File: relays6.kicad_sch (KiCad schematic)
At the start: 1 part

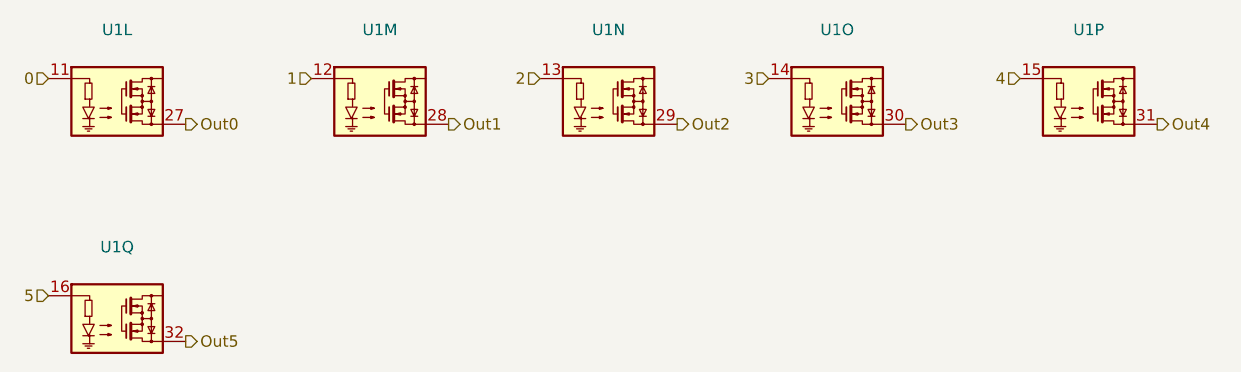
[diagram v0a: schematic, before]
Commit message: added module for PSU
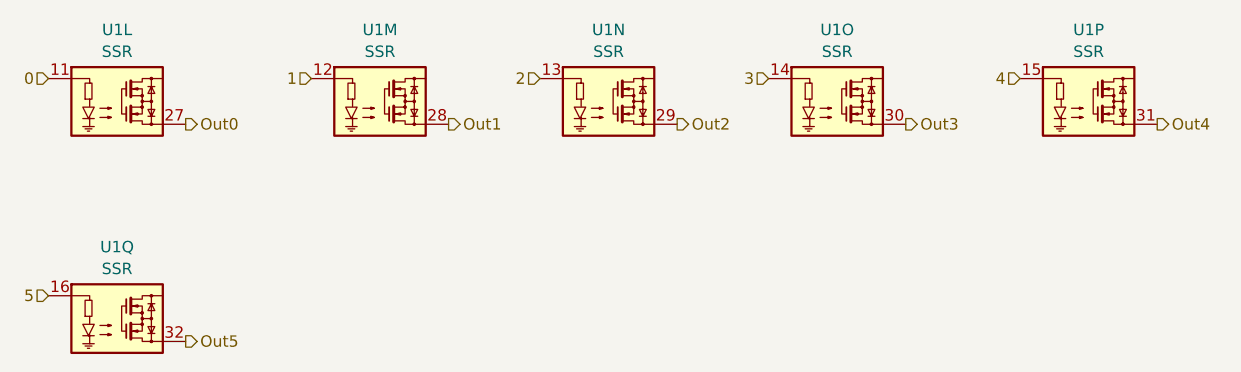
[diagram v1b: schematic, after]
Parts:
- U1: value ~ -> SSR
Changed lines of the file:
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@@
 			)
 		)
-		(property "Value" "~"
+		(property "Value" "SSR"
 			(at 180.34 87.1798 0)
 			(effects
@@
 			)
 		)
-		(property "Value" "~"
+		(property "Value" "SSR"
 			(at 127 87.1798 0)
 			(effects
@@
 			)
 		)
-		(property "Value" "~"
+		(property "Value" "SSR"
 			(at 72.39 111.3098 0)
 			(effects
@@
 			)
 		)
-		(property "Value" "~"
+		(property "Value" "SSR"
 			(at 152.4 87.1798 0)
 			(effects
@@
 			)
 		)
-		(property "Value" "~"
+		(property "Value" "SSR"
 			(at 72.39 87.1798 0)
 			(effects
@@
 			)
 		)
-		(property "Value" "~"
+		(property "Value" "SSR"
 			(at 101.6 87.1798 0)
 			(effects
